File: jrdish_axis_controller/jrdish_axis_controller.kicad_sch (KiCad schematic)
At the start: 24 parts, among them J1 Conn_ARM_SWD_TagConnect_TC2030, SW1 DSHP04TSGER, U1 STM32G474RET6, X1 NX2016SA-16MHZ-EXS00A-CS07826

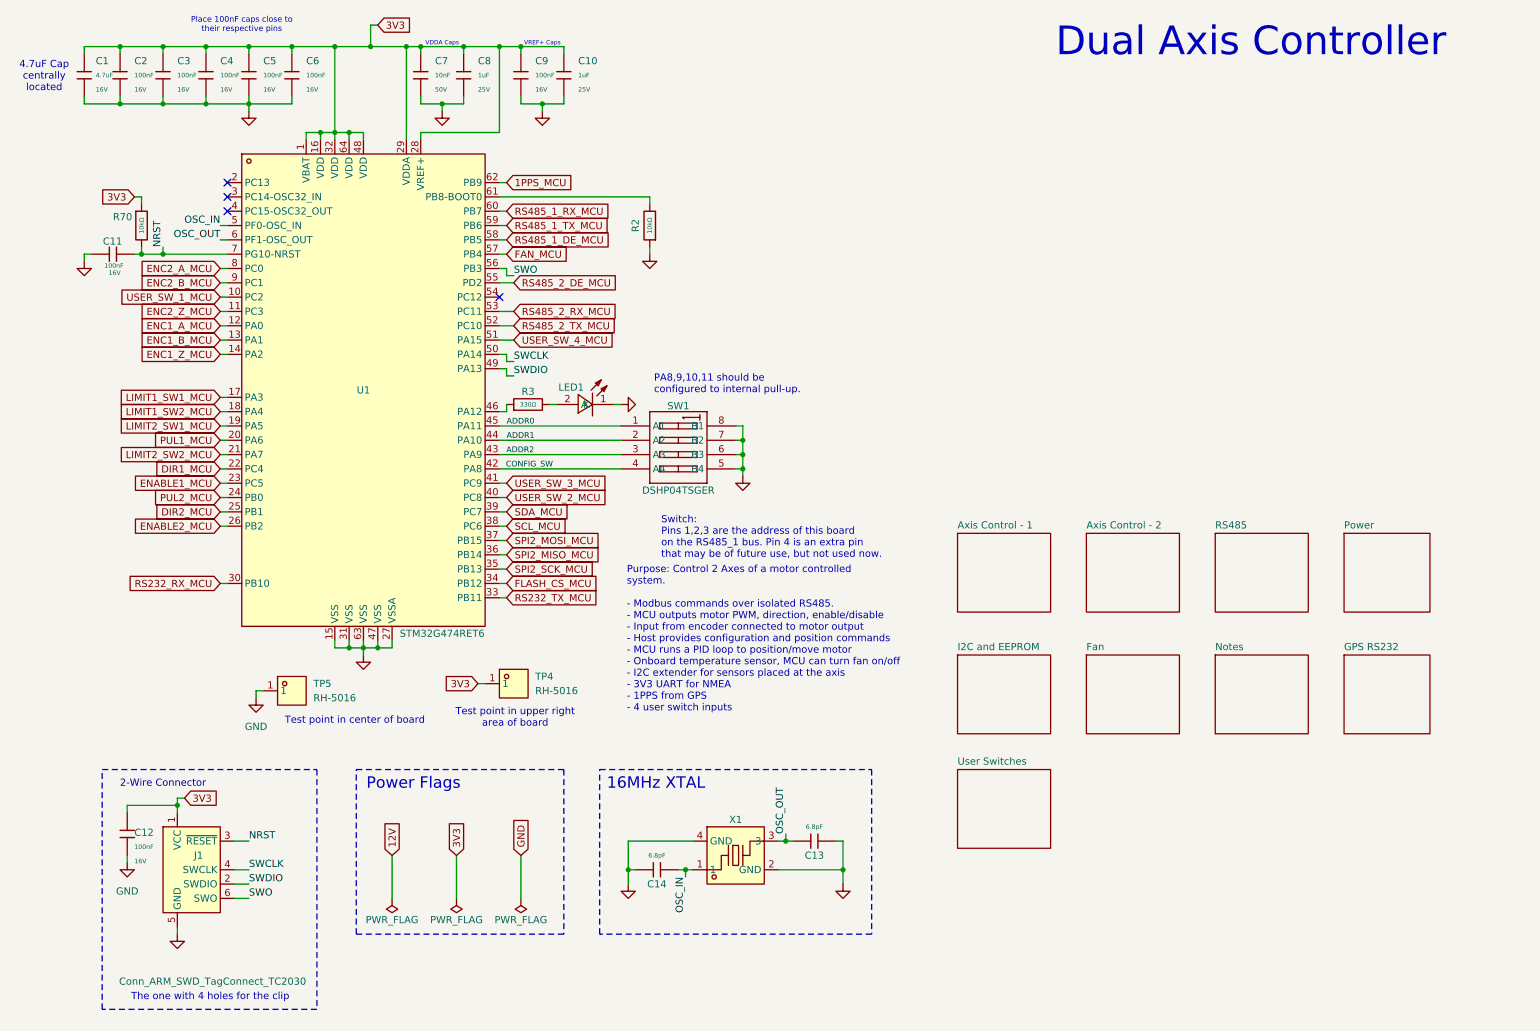
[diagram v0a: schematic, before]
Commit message: Updates for replacing 10k resistors and encoder RC.
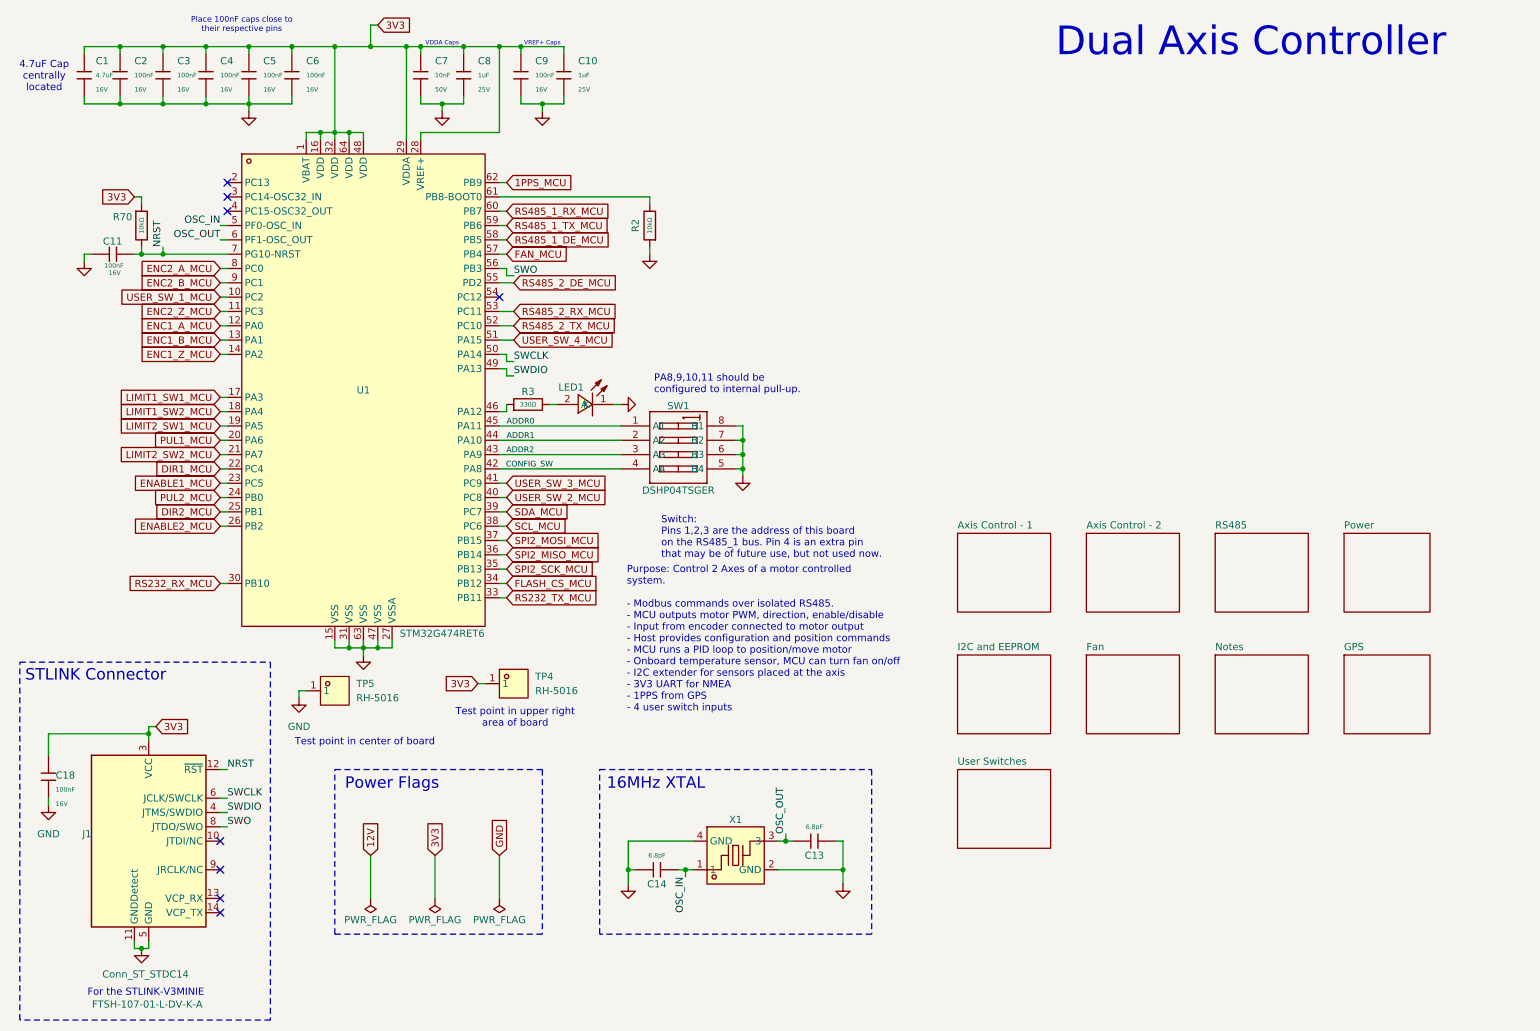
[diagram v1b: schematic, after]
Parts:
- removed C12: 100nF, PCM_JLCPCB:C_0402, symbol PCM_JLCPCB-Capacitors:0402,100nF
- removed J1: Conn_ARM_SWD_TagConnect_TC2030, Connector:Tag-Connect_TC2030-IDC-FP_2x03_P1.27mm_Vertical, symbol Connector:Conn_ARM_SWD_TagConnect_TC2030
- added C18: 100nF, PCM_JLCPCB:C_0402, symbol PCM_JLCPCB-Capacitors:0402,100nF
- added J1: Conn_ST_STDC14, MyParts:HDR-SMD_14P-P1.27_FTSH-107-01-L-DV-K, symbol Connector:Conn_ST_STDC14
- R2: LCSC C25744 -> C173683
- R70: Field4 (none) -> ${REFERENCE}; LCSC C25744 -> C173683
- U1: Manufacturer ST -> ST(意法半导体)
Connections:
- net 3V3: now also C18.1, J1.3 (VCC)
- net GND: now also C18.2, J1.11 (GNDDetect), J1.5 (GND), J1.7 (GND)
- net NRST: now also J1.12 (~{RST})
- net SWCLK: now also J1.6 (JCLK/SWCLK)
- net SWDIO: now also J1.4 (JTMS/SWDIO)
- net SWO: now also J1.8 (JTDO/SWO)
- no-connect marks 4 -> 8
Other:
- sheet GPS RS232 renamed GPS
- note added: "For the STLINK-V3MINIE"
- note removed: "2-Wire Connector"
- note removed: "The one with 4 holes for the clip"
- moved on the sheet: TP5
